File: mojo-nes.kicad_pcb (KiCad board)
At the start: 2 copper layers, 99.7 x 40.9 mm, 9 parts, among them J1 NES-CART, U1 27C512, U2 27C512, U3 ATTINY13-P

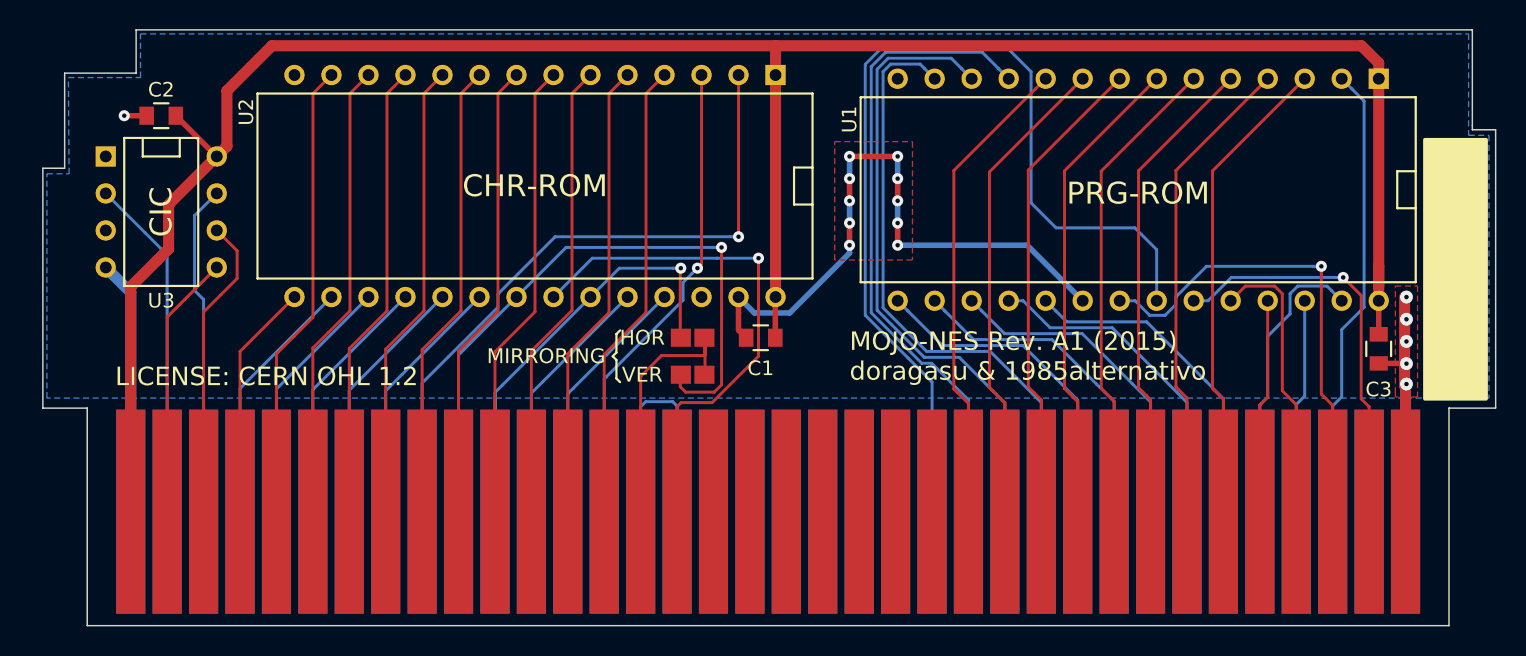
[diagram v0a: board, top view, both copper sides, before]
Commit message: Updated to KiCad v9
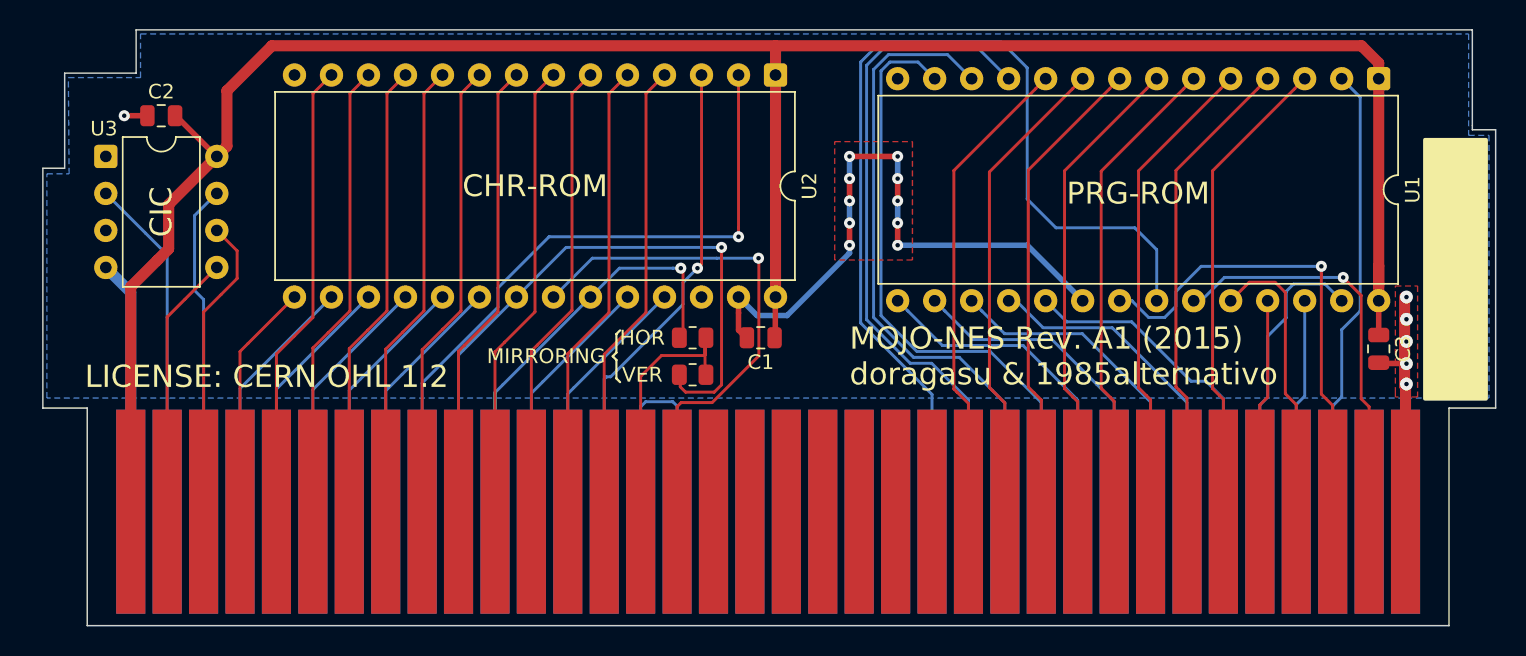
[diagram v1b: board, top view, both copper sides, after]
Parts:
- C1, C2, C3: footprint Capacitors_SMD:C_0805 -> Capacitor_SMD:C_0805_2012Metric
- JP1, JP2: footprint doragasu:JUMPER_0805 -> Resistor_SMD:R_0805_2012Metric
- U1, U2: footprint Sockets_DIP:DIP-28__600 -> Package_DIP:DIP-28_W15.24mm
- U3: footprint Sockets_DIP:DIP-8__300 -> Package_DIP:DIP-8_W7.62mm
- moved U1 18.2 mm to (184.2, 94.7), turned to -90 degrees
- moved U2 18.2 mm to (142.7, 94.5), turned to -90 degrees
- moved U3 5.38 mm to (96.8, 100.1), turned to 0 degrees
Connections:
- J1 pad 14: Net-(J1-Pad14) -> unconnected-(J1-R/~{W}-Pad14)
- J1 pad 15: Net-(J1-Pad15) -> unconnected-(J1-~{IRQ}-Pad15)
- J1 pad 16: Net-(J1-Pad16) -> unconnected-(J1-EXP0-Pad16)
- J1 pad 17: Net-(J1-Pad17) -> unconnected-(J1-EXP1-Pad17)
- J1 pad 18: Net-(J1-Pad18) -> unconnected-(J1-EXP2-Pad18)
- J1 pad 19: Net-(J1-Pad19) -> unconnected-(J1-EXP3-Pad19)
- J1 pad 20: Net-(J1-Pad20) -> unconnected-(J1-EXP4-Pad20)
- J1 pad 37: Net-(J1-Pad37) -> unconnected-(J1-21.48MHz-Pad37)
- J1 pad 38: Net-(J1-Pad38) -> unconnected-(J1-PHI2-Pad38)
- J1 pad 51: Net-(J1-Pad51) -> unconnected-(J1-EXP9-Pad51)
- J1 pad 52: Net-(J1-Pad52) -> unconnected-(J1-EXP8-Pad52)
- J1 pad 53: Net-(J1-Pad53) -> unconnected-(J1-EXP7-Pad53)
- J1 pad 54: Net-(J1-Pad54) -> unconnected-(J1-EXP6-Pad54)
- J1 pad 55: Net-(J1-Pad55) -> unconnected-(J1-EXP5-Pad55)
- J1 pad 56: Net-(J1-Pad56) -> unconnected-(J1-~{W}-Pad56)
- U3 pad 1: Net-(U3-Pad1) -> unconnected-(U3-PB5(~{RESET}/ADC0/PCINT5/dW)-Pad1)
- U3 pad 3: Net-(U3-Pad3) -> unconnected-(U3-PB4(ADC2/PCINT4)-Pad3)
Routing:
- net /PD0: track 44.3 -> 45.5 mm
- net /PD1: track 42.8 -> 43.8 mm
- net /POE: track 67.7 -> 68.5 mm
- net /PD2: track 41.4 -> 42.2 mm
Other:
- net class Default removed
- net class Fat removed
- net class Power removed
